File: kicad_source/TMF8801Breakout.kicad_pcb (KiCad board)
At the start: 2 copper layers, 28 x 20 mm, 28 parts, among them CN1 CONN_01X06, CN2 CONN_01X07, CN3 SM05B-SRSS-TB, Q1 BSS138, Q2 BSS138, Q3 BSS138, U1 MIC5225-3.3, U2 TMF8801

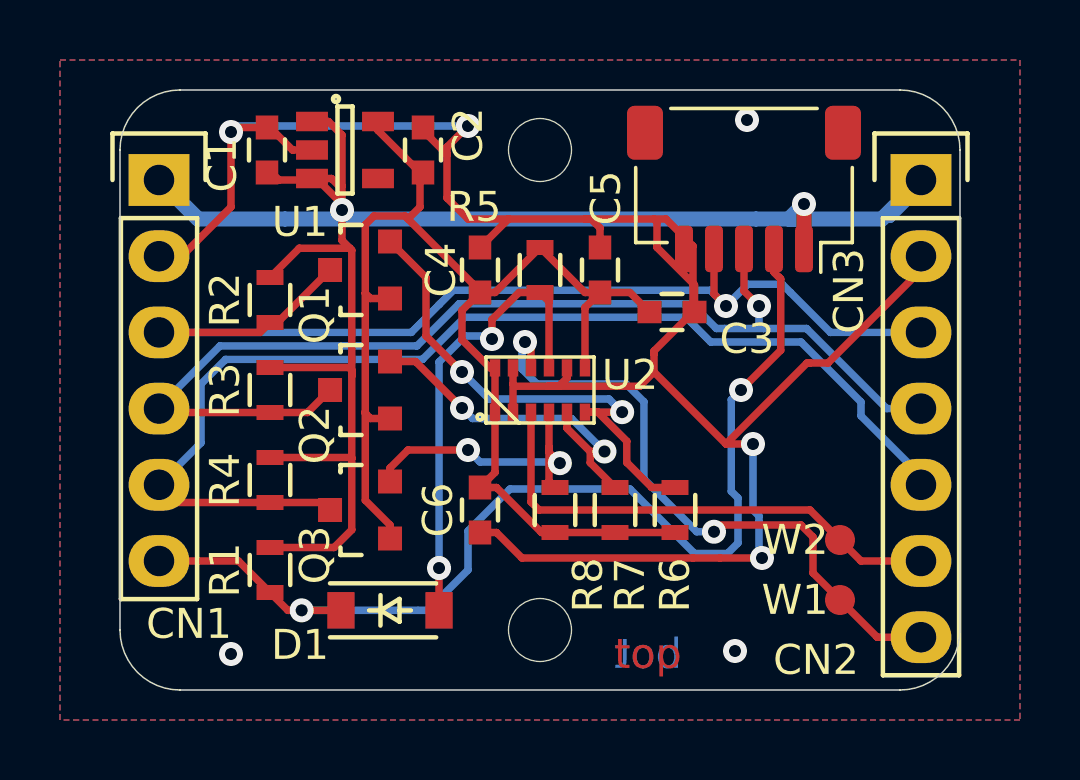
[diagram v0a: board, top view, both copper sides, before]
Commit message: added second ESLOV connector
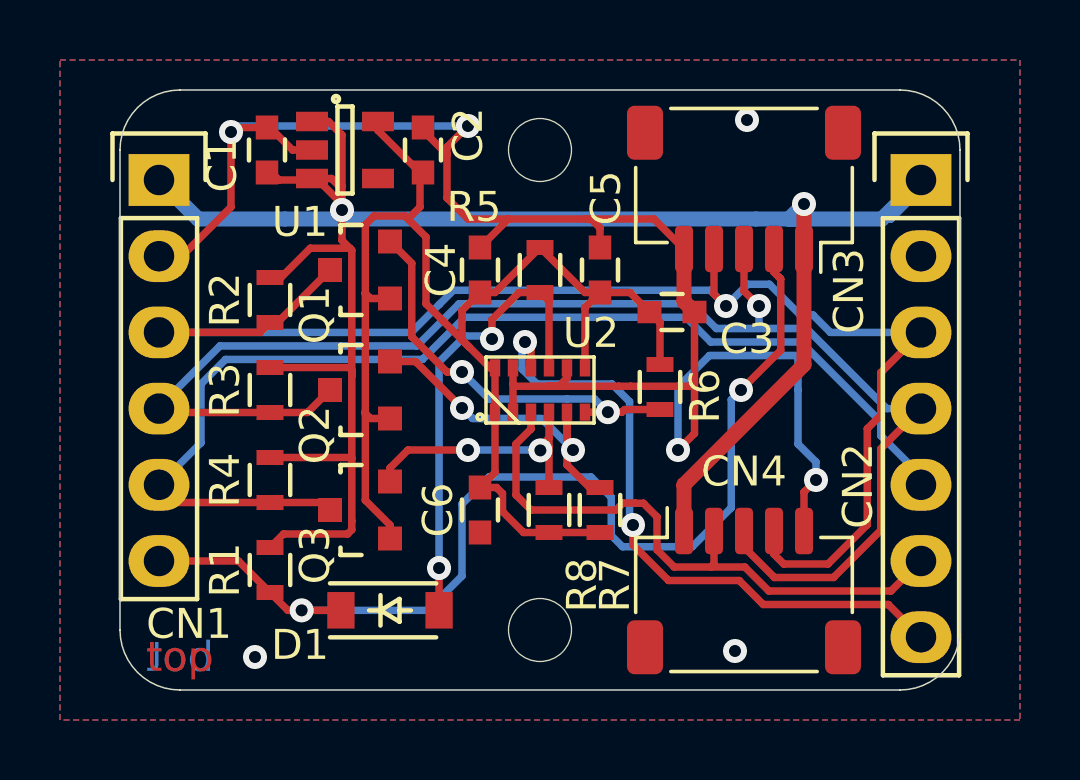
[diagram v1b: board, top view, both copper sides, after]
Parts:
- removed W1, W2: TEST_1P, wire_pads:SolderWirePad_single_1mmSMD
- added CN4: SM05B-SRSS-TB, Connector_JST:JST_SH_SM05B-SRSS-TB_1x05-1MP_P1.00mm_Horizontal, F.Cu at (171.8, 122.7)
- moved R6 4.13 mm to (169.0, 115.9), turned to 270 degrees
- moved R7 0.50 mm to (167.0, 120.0)
- moved R8 0.20 mm to (165.3, 120.0)
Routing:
- net GND: track 75.4 -> 60.3 mm
- net VCC: track 81.9 -> 94.5 mm
- net /I2C_SDA_5V: track 36.4 -> 48.1 mm
- net /I2C_SCL_5V: track 37.9 -> 48.7 mm
- net /I2C_SDA: track 16.9 -> 13.6 mm
- net /GPIO0: track 17.1 -> 20.3 mm
- net /INT: track 9.82 -> 8.84 mm
- net +3V3: track 46.6 -> 47.6 mm
- net /EN_5V: track 35.4 -> 36.0 mm
